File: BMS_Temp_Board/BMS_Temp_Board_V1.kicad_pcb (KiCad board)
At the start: 4 copper layers, 68 x 83.4 mm, 71 parts, among them IC1 ESP32-S3-WROOM-1-N8R8, IC2 CP2102N-A02-GQFN28, IC3 TLP175A_TPL,E, IC4 TPS2116DRLR, IC5 MIC37100-3.3WS, IC6 CD74HC4067PWR, IC7 CD74HC4067PWR, IC8 CD74HC4067PWR, IC9 CD74HC4067PWR, J1 ESP_USB, J2 B32B-PUDSS-1_LF__SN_, J3 B32B-PUDSS-1_LF__SN_, J4 B32B-PUDSS-1_LF__SN_, J5 B32B-PUDSS-1_LF__SN_, J6 776279-1, Q1 MMBT2222LT1G, Q2 MMBT2222LT1G, Q3 LTV-817S-TA1, U1 USBLC6-2SC6, U2 SN65HVD230, U3 LM2575HVS-5.0_NOPB

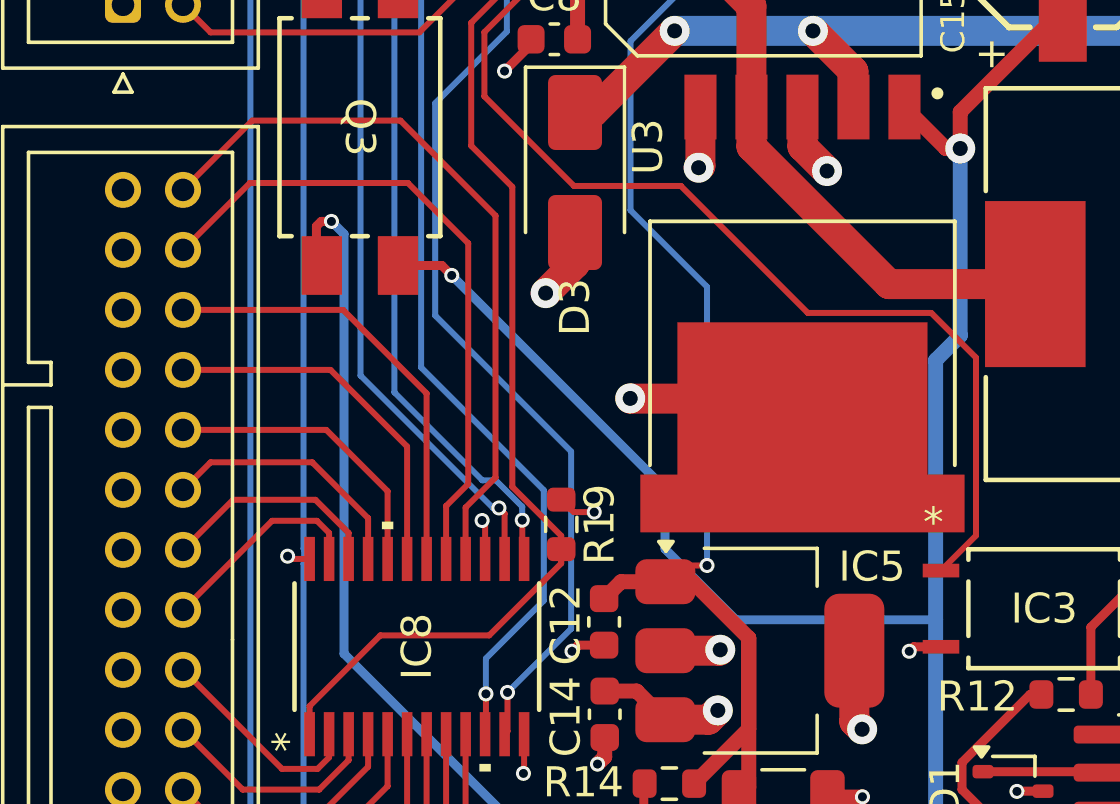
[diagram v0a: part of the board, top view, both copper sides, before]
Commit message: Added resistor and capacitor to optoisolator
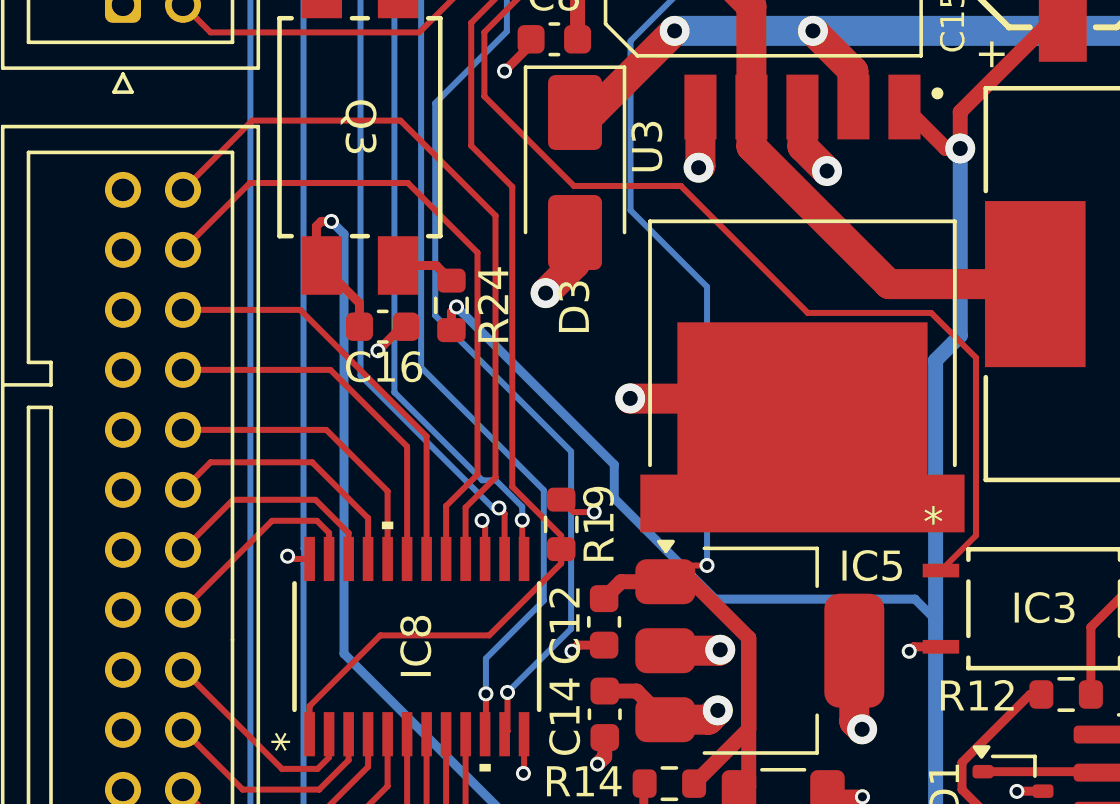
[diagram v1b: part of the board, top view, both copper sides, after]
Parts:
- added C16: 0.1uF, Capacitor_SMD:C_0603_1608Metric, F.Cu at (93.3, 119.1)
- added R24: 10k, Resistor_SMD:R_0603_1608Metric, F.Cu at (95.6, 118.4)
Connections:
- Q3 pad 4: +12V -> Net-(Q3-Pad4)
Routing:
- net /SHUTOFF_ISO: track 47.4 -> 50.0 mm
- net +12V: track 84.2 -> 82.0 mm
- net Net-(Q3-Pad4): track 0.00 -> 1.99 mm
- net GND: track 87.0 -> 88.2 mm, vias 60 -> 61
- net Net-(IC8-I13): track 14.8 -> 14.0 mm
